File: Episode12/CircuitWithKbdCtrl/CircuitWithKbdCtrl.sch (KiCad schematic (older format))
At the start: 0 parts

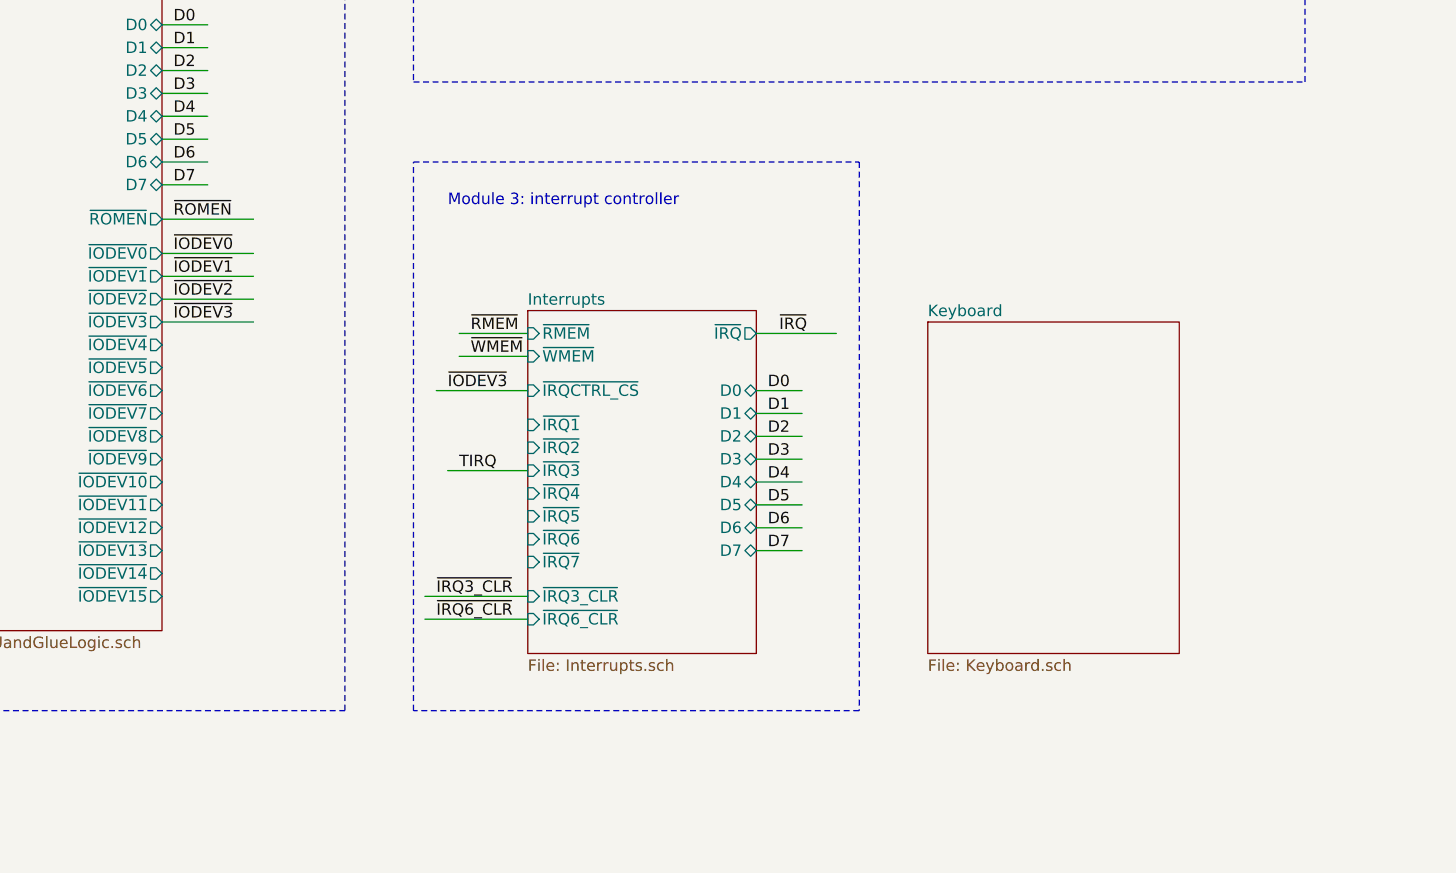
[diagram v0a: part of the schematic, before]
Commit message: made connections to keyboard controller
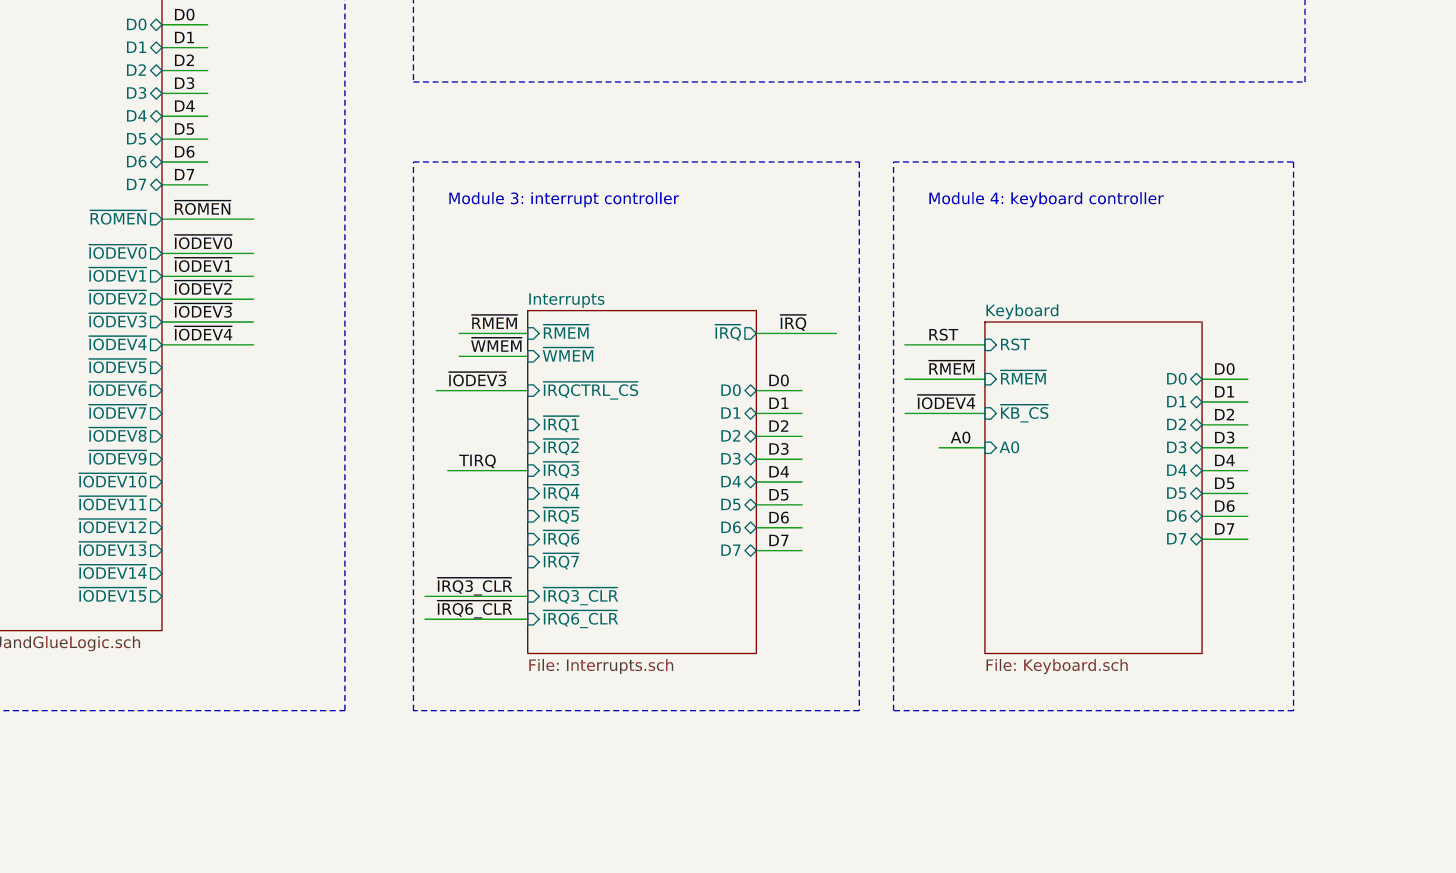
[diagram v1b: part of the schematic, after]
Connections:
- net labels added: ~IODEV4
- wire segments 98 -> 111
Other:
- note added: "Module 4: keyboard controller"
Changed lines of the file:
@@
 ~IRQ6_CLR
 $Sheet
-S 6550 5400 1100 1450
+S 6800 5400 950  1450
 U 5E2CF983
 F0 "Keyboard" 50
 F1 "Keyboard.sch" 50
+F2 "A0" I L 6800 5950 50
+F3 "~RMEM" I L 6800 5650 50
+F4 "~KB_CS" I L 6800 5800 50
+F5 "D0" B R 7750 5650 50
+F6 "D1" B R 7750 5750 50
+F7 "D2" B R 7750 5850 50
+F8 "D3" B R 7750 5950 50
+F9 "D4" B R 7750 6050 50
+F10 "D5" B R 7750 6150 50
+F11 "D6" B R 7750 6250 50
+F12 "D7" B R 7750 6350 50
+F13 "RST" I L 6800 5500 50
 $EndSheet
+Wire Wire Line
+	6450 5500 6800 5500
+Text Label 6550 5500 0    50   ~ 0
+RST
+Wire Notes Line
+	6400 4700 8150 4700
+Wire Notes Line
+	8150 4700 8150 7100
+Wire Notes Line
+	8150 7100 6400 7100
+Wire Notes Line
+	6400 7100 6400 4700
+Text Notes 6550 4900 0    50   ~ 0
+Module 4: keyboard controller
+Wire Wire Line
+	7750 5650 7950 5650
+Wire Wire Line
+	7750 5750 7950 5750
+Wire Wire Line
+	7750 5850 7950 5850
+Wire Wire Line
+	7750 5950 7950 5950
+Wire Wire Line
+	7750 6050 7950 6050
+Wire Wire Line
+	7750 6150 7950 6150
+Wire Wire Line
+	7750 6250 7950 6250
+Wire Wire Line
+	7750 6350 7950 6350
+Text Label 7800 5650 0    50   ~ 0
+D0
+Text Label 7800 5750 0    50   ~ 0
+D1
+Text Label 7800 5850 0    50   ~ 0
+D2
+Text Label 7800 5950 0    50   ~ 0
+D3
+Text Label 7800 6050 0    50   ~ 0
+D4
+Text Label 7800 6150 0    50   ~ 0
+D5
+Text Label 7800 6250 0    50   ~ 0
+D6
+Text Label 7800 6350 0    50   ~ 0
+D7
+Wire Wire Line
+	6450 5650 6800 5650
+Text Label 6550 5650 0    50   ~ 0
+~RMEM~
+Wire Wire Line
+	3200 5500 3600 5500
+Text Label 3250 5500 0    50   ~ 0
+~IODEV4
+Wire Wire Line
+	6450 5800 6800 5800
+Text Label 6500 5800 0    50   ~ 0
+~IODEV4
+Wire Wire Line
+	6600 5950 6800 5950
+Text Label 6650 5950 0    50   ~ 0
+A0
 $EndSCHEMATC
